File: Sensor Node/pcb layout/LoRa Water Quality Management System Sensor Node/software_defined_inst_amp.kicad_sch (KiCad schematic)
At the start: 25 parts, among them U13 MCP4651T-503E_ST, U14 LMV324, U15 MCP4651T-503E_ST, U16 MCP4651T-503E_ST

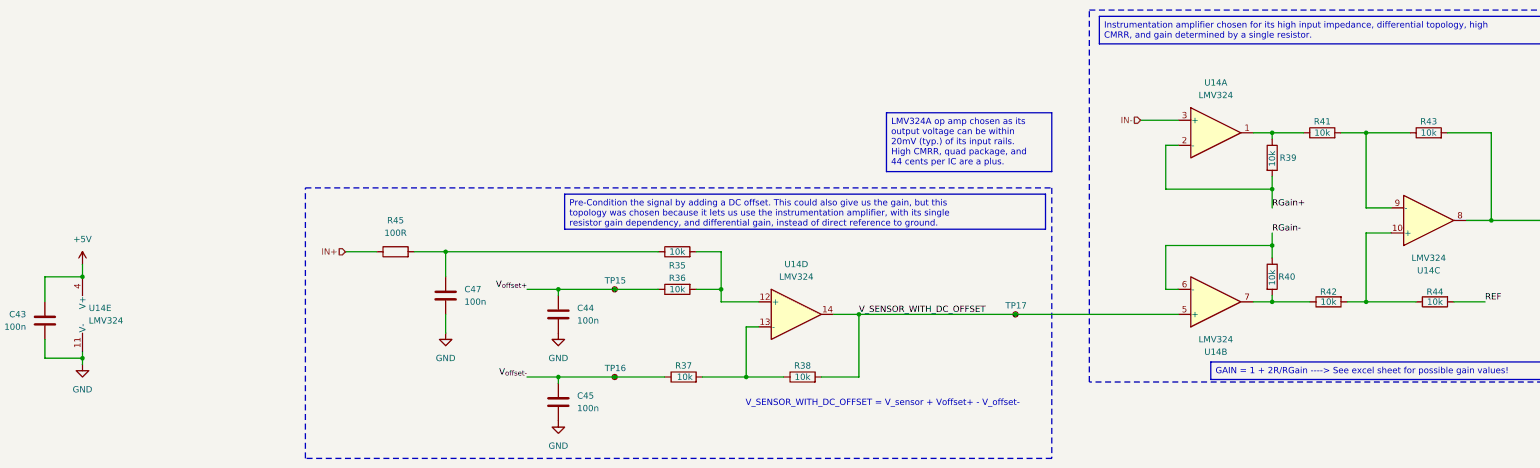
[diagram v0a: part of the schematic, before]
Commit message: Finalize working software-defined instrumentation amplifier driver code and signal acquisition, begin prototyping sensor data conversion methods. Add hardware changes needed for expected operation of analog front-end.
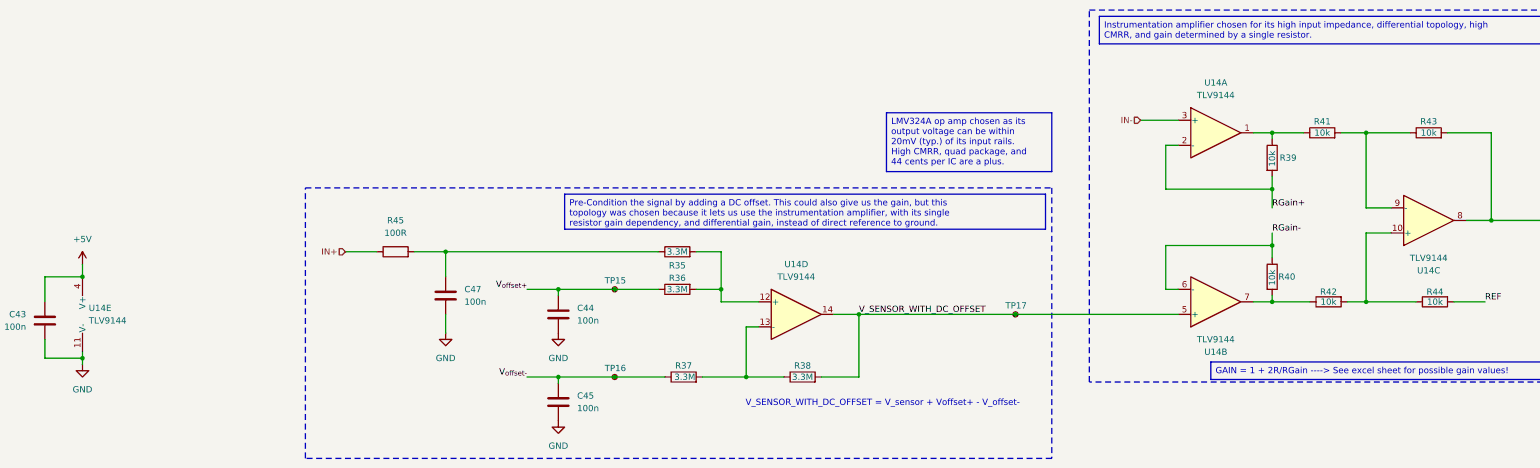
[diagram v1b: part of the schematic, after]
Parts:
- R35, R36, R37, R38: value 10k -> 3.3M
- U14: value LMV324 -> TLV9144
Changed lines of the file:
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@@
 			)
 		)
-		(property "Value" "LMV324"
+		(property "Value" "TLV9144"
 			(at 85.09 222.2499 0)
 			(effects
@@
 			)
 		)
-		(property "Value" "10k"
+		(property "Value" "3.3M"
 			(at 204.47 208.28 90)
 			(effects
@@
 			)
 		)
-		(property "Value" "10k"
+		(property "Value" "3.3M"
 			(at 204.47 215.9 90)
 			(effects
@@
 			)
 		)
-		(property "Value" "10k"
+		(property "Value" "3.3M"
 			(at 205.994 233.68 90)
 			(effects
@@
 			)
 		)
-		(property "Value" "LMV324"
+		(property "Value" "TLV9144"
 			(at 313.69 176.53 0)
 			(effects
@@
 			)
 		)
-		(property "Value" "LMV324"
+		(property "Value" "TLV9144"
 			(at 228.6 213.36 0)
 			(effects
@@
 			)
 		)
-		(property "Value" "10k"
+		(property "Value" "3.3M"
 			(at 229.87 233.68 90)
 			(effects
@@
 			)
 		)
-		(property "Value" "LMV324"
+		(property "Value" "TLV9144"
 			(at 356.87 209.55 0)
 			(effects
@@
 			)
 		)
-		(property "Value" "LMV324"
+		(property "Value" "TLV9144"
 			(at 313.69 226.06 0)
 			(effects
